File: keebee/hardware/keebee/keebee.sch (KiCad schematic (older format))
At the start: 2 parts

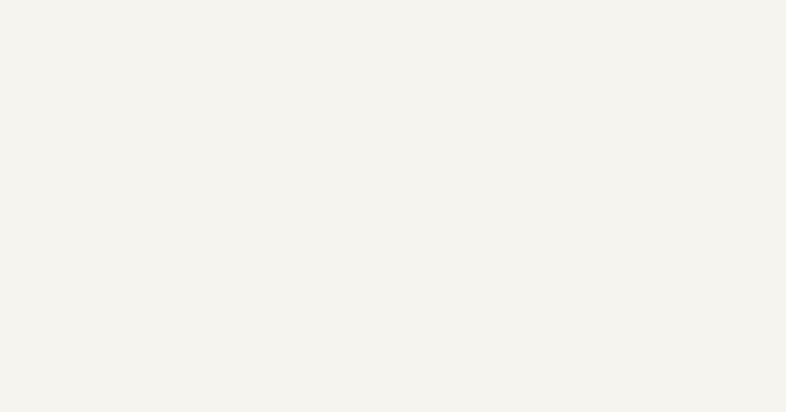
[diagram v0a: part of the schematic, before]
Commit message: Add in keebee power schematic
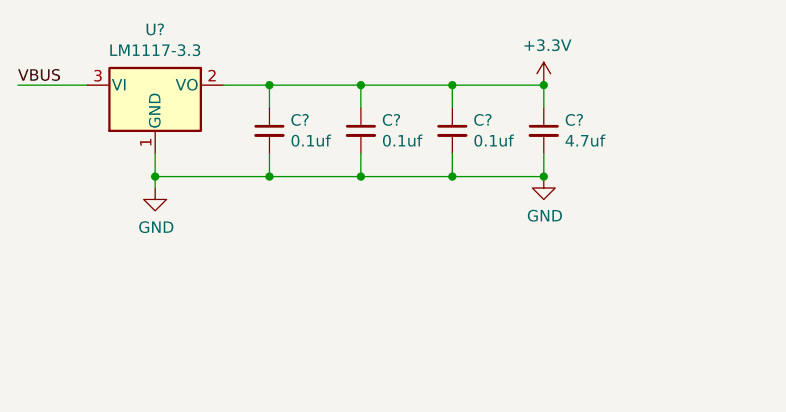
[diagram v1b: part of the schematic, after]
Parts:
- added C? (x3): 0.1uf, symbol Device:C_Small
- added C?: 4.7uf, symbol Device:C_Small
- added U?: LM1117-3.3, symbol Regulator_Linear:LM1117-3.3
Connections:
- net +3V3: now also C?.1, C?.1, C?.1, C?.1, U?.2 (VO)
- net GND: now also C?.2, C?.2, C?.2, C?.2, U?.1 (GND)
- net VBUS: now also U?.3 (VI)
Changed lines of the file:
@@
 Text Label 4700 3500 0    50   ~ 0
 ROW0
+$Comp
+L Regulator_Linear:LM1117-3.3 U?
+U 1 1 5B310EFD
+P 2050 1150
+F 0 "U?" H 2050 1392 50  0000 C CNN
+F 1 "LM1117-3.3" H 2050 1301 50  0000 C CNN
+F 2 "" H 2050 1150 50  0001 C CNN
+F 3 "http://www.ti.com/lit/ds/symlink/lm1117.pdf" H 2050 1150 50  0001 C CNN
+	1    2050 1150
+	1    0    0    -1
+$EndComp
+Wire Wire Line
+	1750 1150 1450 1150
+Text Label 1450 1150 0    50   ~ 0
+VBUS
+$Comp
+L power:+3.3V #PWR?
+U 1 1 5B312C80
+P 3750 1150
+F 0 "#PWR?" H 3750 1000 50  0001 C CNN
+F 1 "+3.3V" H 3765 1323 50  0000 C CNN
+F 2 "" H 3750 1150 50  0001 C CNN
+F 3 "" H 3750 1150 50  0001 C CNN
+	1    3750 1150
+	1    0    0    -1
+$EndComp
+Wire Wire Line
+	2050 1450 2050 1550
+$Comp
+L power:GND #PWR?
+U 1 1 5B313FEA
+P 2050 1600
+F 0 "#PWR?" H 2050 1350 50  0001 C CNN
+F 1 "GND" H 2055 1427 50  0000 C CNN
+F 2 "" H 2050 1600 50  0001 C CNN
+F 3 "" H 2050 1600 50  0001 C CNN
+	1    2050 1600
+	1    0    0    -1
+$EndComp
+Connection ~ 2050 1550
+Wire Wire Line
+	2050 1550 2050 1600
+$Comp
+L power:GND #PWR?
+U 1 1 5B31724A
+P 3750 1550
+F 0 "#PWR?" H 3750 1300 50  0001 C CNN
+F 1 "GND" H 3755 1377 50  0000 C CNN
+F 2 "" H 3750 1550 50  0001 C CNN
+F 3 "" H 3750 1550 50  0001 C CNN
+	1    3750 1550
+	1    0    0    -1
+$EndComp
+$Comp
+L Device:C_Small C?
+U 1 1 5B317DA6
+P 2550 1350
+F 0 "C?" H 2642 1396 50  0000 L CNN
+F 1 "0.1uf" H 2642 1305 50  0000 L CNN
+F 2 "" H 2550 1350 50  0001 C CNN
+F 3 "~" H 2550 1350 50  0001 C CNN
+	1    2550 1350
+	1    0    0    -1
+$EndComp
+$Comp
+L Device:C_Small C?
+U 1 1 5B317DF6
+P 2950 1350
+F 0 "C?" H 3042 1396 50  0000 L CNN
+F 1 "0.1uf" H 3042 1305 50  0000 L CNN
+F 2 "" H 2950 1350 50  0001 C CNN
+F 3 "~" H 2950 1350 50  0001 C CNN
+	1    2950 1350
+	1    0    0    -1
+$EndComp
+$Comp
+L Device:C_Small C?
+U 1 1 5B317E31
+P 3350 1350
+F 0 "C?" H 3442 1396 50  0000 L CNN
+F 1 "0.1uf" H 3442 1305 50  0000 L CNN
+F 2 "" H 3350 1350 50  0001 C CNN
+F 3 "~" H 3350 1350 50  0001 C CNN
+	1    3350 1350
+	1    0    0    -1
+$EndComp
+Wire Wire Line
+	2350 1150 2550 1150
+Wire Wire Line
+	2050 1550 2550 1550
+$Comp
+L Device:C_Small C?
+U 1 1 5B31D042
+P 3750 1350
+F 0 "C?" H 3842 1396 50  0000 L CNN
+F 1 "4.7uf" H 3842 1305 50  0000 L CNN
+F 2 "" H 3750 1350 50  0001 C CNN
+F 3 "~" H 3750 1350 50  0001 C CNN
+	1    3750 1350
+	1    0    0    -1
+$EndComp
+Wire Wire Line
+	3750 1150 3750 1250
+Connection ~ 3750 1150
+Wire Wire Line
+	3750 1450 3750 1550
+Connection ~ 3750 1550
+Wire Wire Line
+	3350 1250 3350 1150
+Connection ~ 3350 1150
+Wire Wire Line
+	3350 1150 3750 1150
+Wire Wire Line
+	3350 1450 3350 1550
+Connection ~ 3350 1550
+Wire Wire Line
+	3350 1550 3750 1550
+Wire Wire Line
+	2950 1250 2950 1150
+Connection ~ 2950 1150
+Wire Wire Line
+	2950 1150 3350 1150
+Wire Wire Line
+	2550 1250 2550 1150
+Connection ~ 2550 1150
+Wire Wire Line
+	2550 1150 2950 1150
+Wire Wire Line
+	2550 1450 2550 1550
+Connection ~ 2550 1550
+Wire Wire Line
+	2550 1550 2950 1550
+Wire Wire Line
+	2950 1450 2950 1550
+Connection ~ 2950 1550
+Wire Wire Line
+	2950 1550 3350 1550
 $EndSCHEMATC

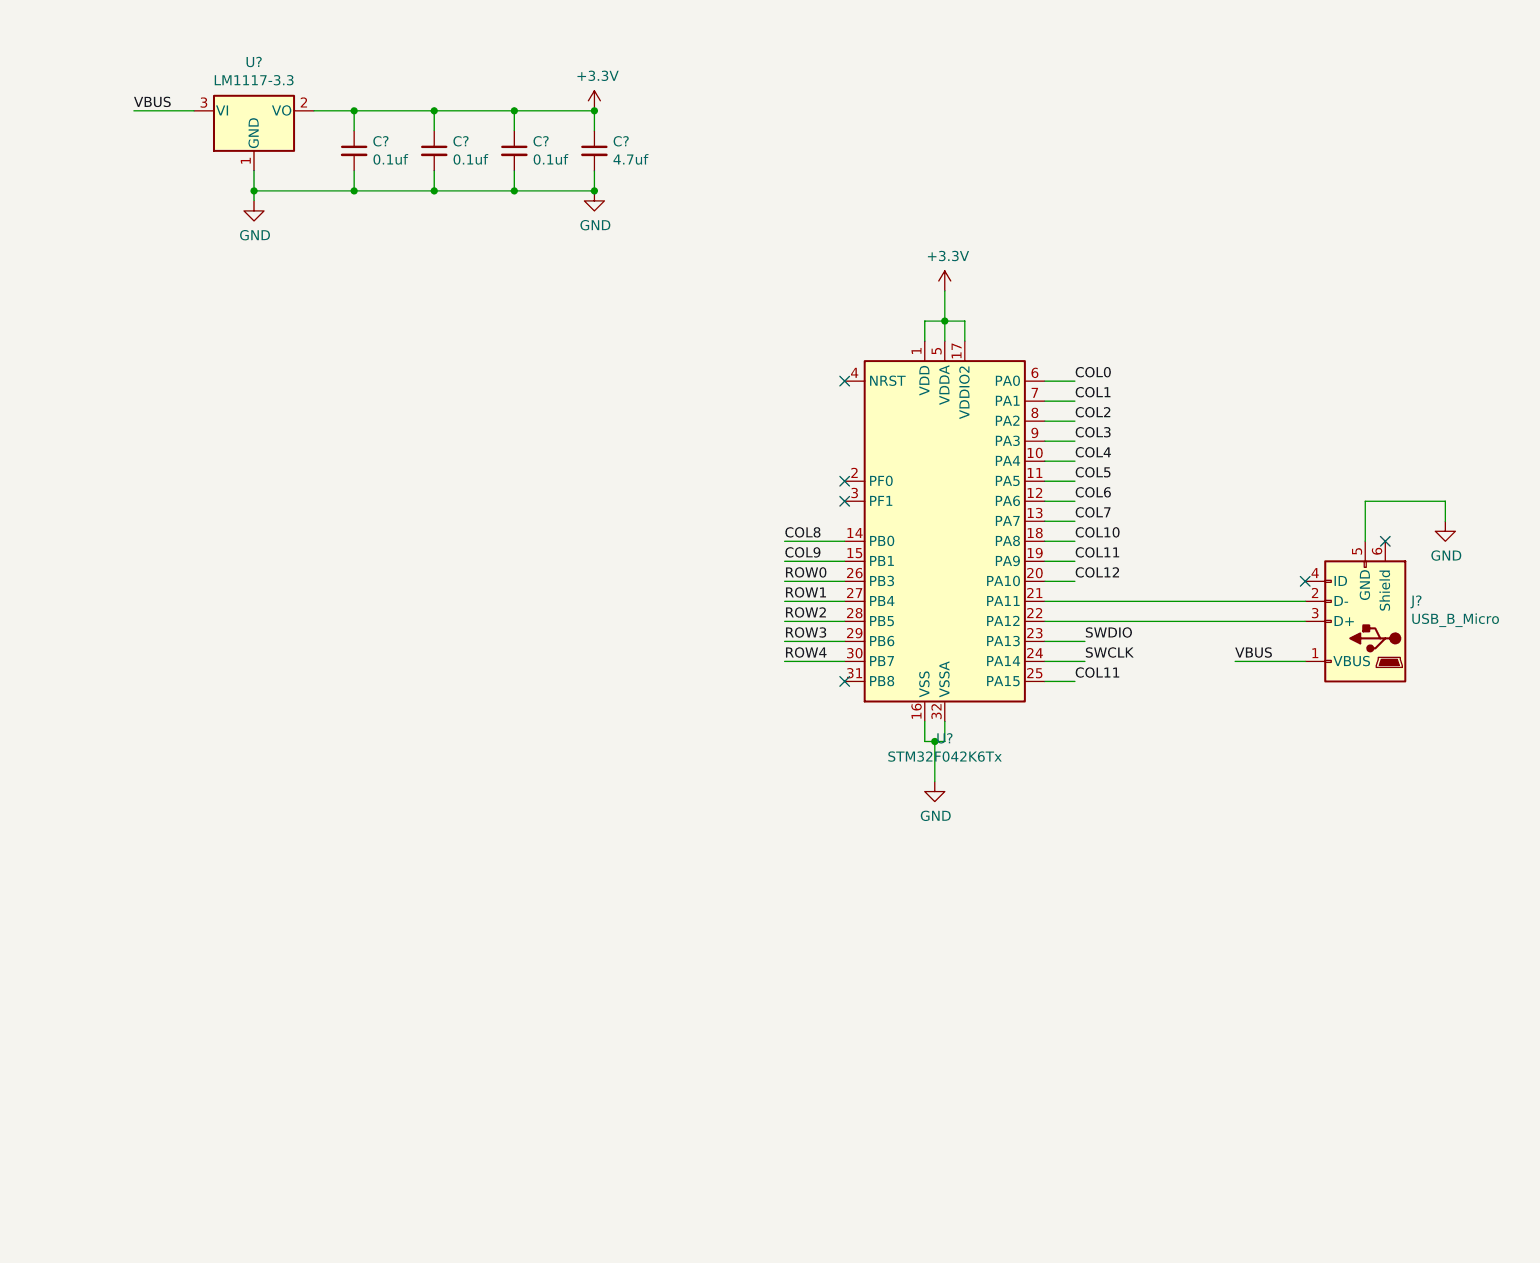
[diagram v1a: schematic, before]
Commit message: Add key matrix sub-sheet
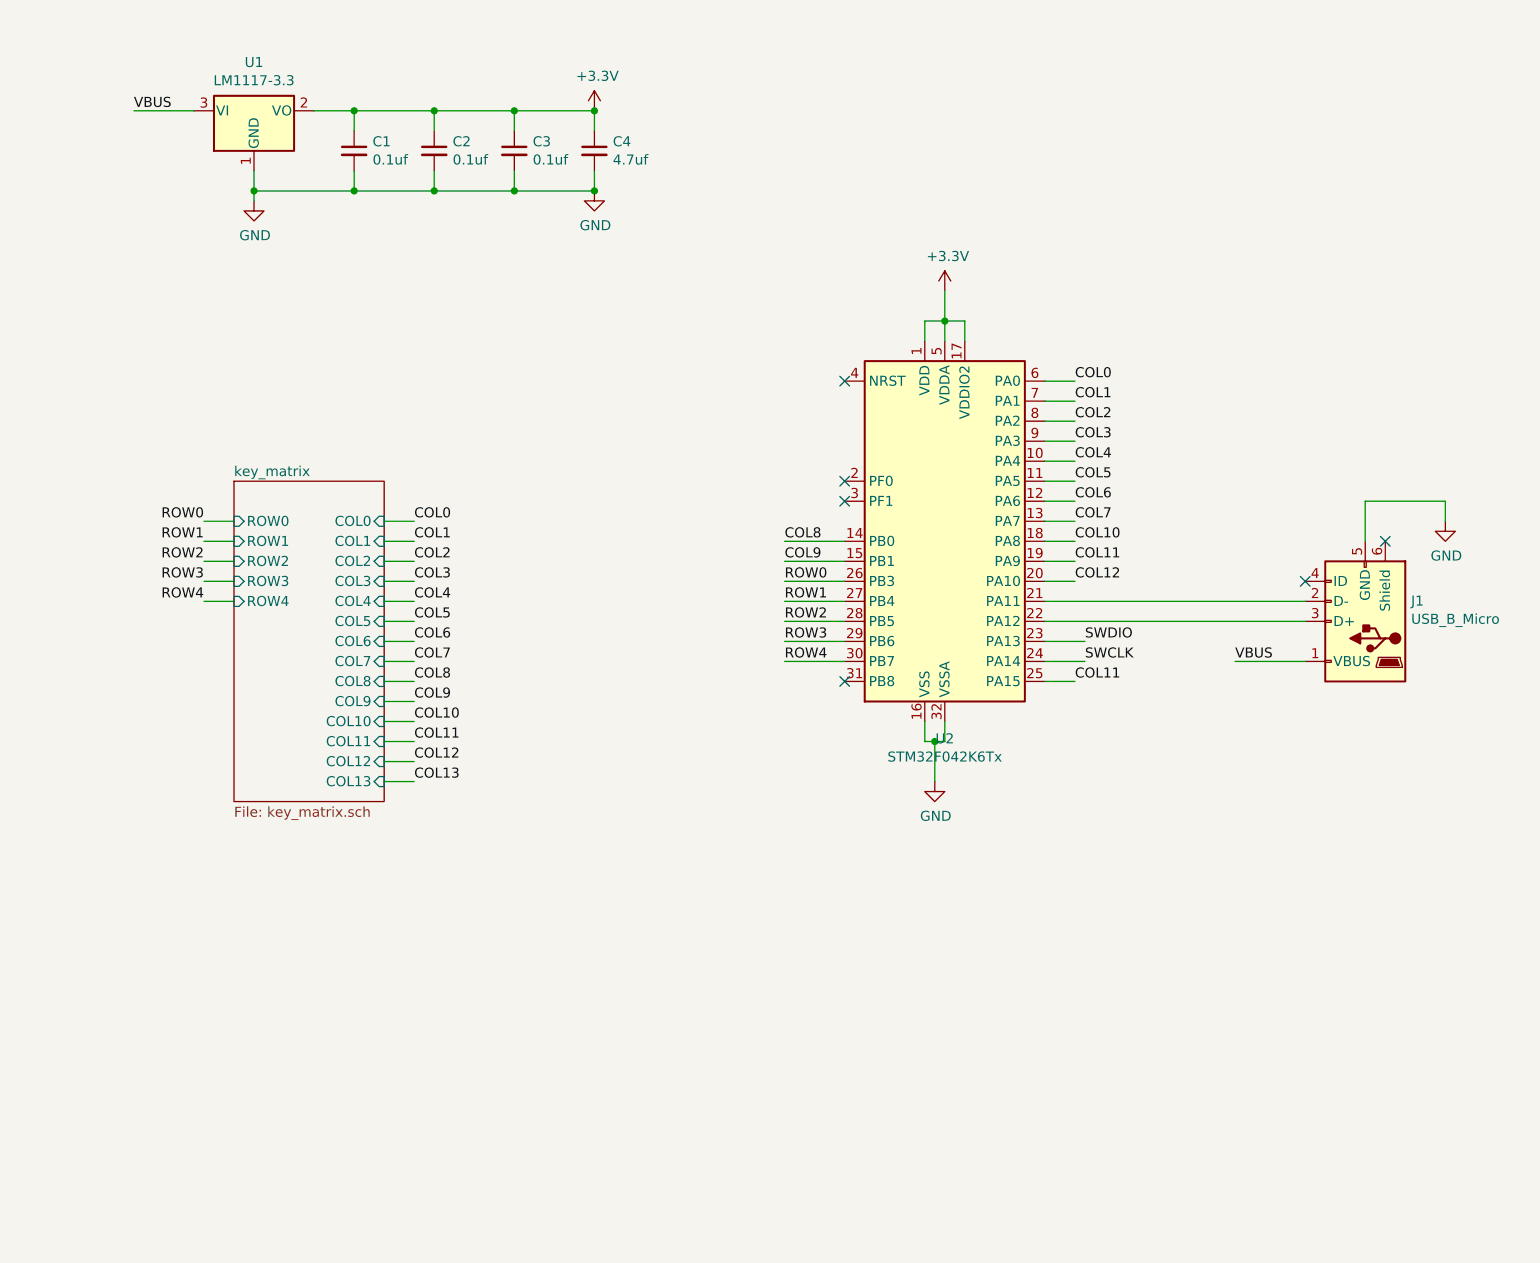
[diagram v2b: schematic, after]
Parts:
- gave numbers to parts that had none: 7
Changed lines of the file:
@@
 $Descr A4 11693 8268
 encoding utf-8
-Sheet 1 1
+Sheet 1 2
 Title ""
 Date ""
@@
 $EndDescr
 $Comp
-L MCU_ST_STM32F0:STM32F042K6Tx U?
+L MCU_ST_STM32F0:STM32F042K6Tx U2
 U 1 1 5B304C68
 P 5500 3200
-F 0 "U?" H 5500 2114 50  0000 C CNN
+F 0 "U2" H 5500 2114 50  0000 C CNN
 F 1 "STM32F042K6Tx" H 5500 2023 50  0000 C CNN
 F 2 "Package_QFP:LQFP-32_7x7mm_P0.8mm" H 5100 2300 50  0001 R CNN
@@
 	5450 4300 5500 4300
 $Comp
-L power:GND #PWR?
+L power:GND #PWR0101
 U 1 1 5B304DF2
 P 5450 4500
-F 0 "#PWR?" H 5450 4250 50  0001 C CNN
+F 0 "#PWR0101" H 5450 4250 50  0001 C CNN
 F 1 "GND" H 5455 4327 50  0000 C CNN
 F 2 "" H 5450 4500 50  0001 C CNN
@@
 	5500 2200 5500 2050
 $Comp
-L power:+3.3V #PWR?
+L power:+3.3V #PWR0102
 U 1 1 5B304F70
 P 5500 2050
-F 0 "#PWR?" H 5500 1900 50  0001 C CNN
+F 0 "#PWR0102" H 5500 1900 50  0001 C CNN
 F 1 "+3.3V" H 5515 2223 50  0000 C CNN
 F 2 "" H 5500 2050 50  0001 C CNN
@@
 SWCLK
 $Comp
-L Connector:USB_B_Micro J?
+L Connector:USB_B_Micro J1
 U 1 1 5B305155
 P 7600 3700
-F 0 "J?" H 7371 3598 50  0000 R CNN
+F 0 "J1" H 7371 3598 50  0000 R CNN
 F 1 "USB_B_Micro" H 7371 3689 50  0000 R CNN
 F 2 "" H 7750 3650 50  0001 C CNN
@@
 	8000 3100 8000 3200
 $Comp
-L power:GND #PWR?
+L power:GND #PWR0103
 U 1 1 5B3057C1
 P 8000 3200
-F 0 "#PWR?" H 8000 2950 50  0001 C CNN
+F 0 "#PWR0103" H 8000 2950 50  0001 C CNN
 F 1 "GND" H 8005 3027 50  0000 C CNN
 F 2 "" H 8000 3200 50  0001 C CNN
@@
 Wire Wire Line
 	4700 3400 5000 3400
-Wire Wire Line
-	4700 3500 5000 3500
-Wire Wire Line
-	4700 3600 5000 3600
-Wire Wire Line
-	4700 3700 5000 3700
-Wire Wire Line
-	4700 3800 5000 3800
-Wire Wire Line
-	4700 3900 5000 3900
 NoConn ~ 5000 2500
 NoConn ~ 5000 3000
@@
 ROW0
 $Comp
-L Regulator_Linear:LM1117-3.3 U?
+L Regulator_Linear:LM1117-3.3 U1
 U 1 1 5B310EFD
 P 2050 1150
-F 0 "U?" H 2050 1392 50  0000 C CNN
+F 0 "U1" H 2050 1392 50  0000 C CNN
 F 1 "LM1117-3.3" H 2050 1301 50  0000 C CNN
 F 2 "" H 2050 1150 50  0001 C CNN
@@
 VBUS
 $Comp
-L power:+3.3V #PWR?
+L power:+3.3V #PWR0104
 U 1 1 5B312C80
 P 3750 1150
-F 0 "#PWR?" H 3750 1000 50  0001 C CNN
+F 0 "#PWR0104" H 3750 1000 50  0001 C CNN
 F 1 "+3.3V" H 3765 1323 50  0000 C CNN
 F 2 "" H 3750 1150 50  0001 C CNN
@@
 	2050 1450 2050 1550
 $Comp
-L power:GND #PWR?
+L power:GND #PWR0105
 U 1 1 5B313FEA
 P 2050 1600
-F 0 "#PWR?" H 2050 1350 50  0001 C CNN
+F 0 "#PWR0105" H 2050 1350 50  0001 C CNN
 F 1 "GND" H 2055 1427 50  0000 C CNN
 F 2 "" H 2050 1600 50  0001 C CNN
@@
 	2050 1550 2050 1600
 $Comp
-L power:GND #PWR?
+L power:GND #PWR0106
 U 1 1 5B31724A
 P 3750 1550
-F 0 "#PWR?" H 3750 1300 50  0001 C CNN
+F 0 "#PWR0106" H 3750 1300 50  0001 C CNN
 F 1 "GND" H 3755 1377 50  0000 C CNN
 F 2 "" H 3750 1550 50  0001 C CNN
@@
 $EndComp
 $Comp
-L Device:C_Small C?
+L Device:C_Small C1
 U 1 1 5B317DA6
 P 2550 1350
-F 0 "C?" H 2642 1396 50  0000 L CNN
+F 0 "C1" H 2642 1396 50  0000 L CNN
 F 1 "0.1uf" H 2642 1305 50  0000 L CNN
 F 2 "" H 2550 1350 50  0001 C CNN
@@
 $EndComp
 $Comp
-L Device:C_Small C?
+L Device:C_Small C2
 U 1 1 5B317DF6
 P 2950 1350
-F 0 "C?" H 3042 1396 50  0000 L CNN
+F 0 "C2" H 3042 1396 50  0000 L CNN
 F 1 "0.1uf" H 3042 1305 50  0000 L CNN
 F 2 "" H 2950 1350 50  0001 C CNN
@@
 $EndComp
 $Comp
-L Device:C_Small C?
+L Device:C_Small C3
 U 1 1 5B317E31
 P 3350 1350
-F 0 "C?" H 3442 1396 50  0000 L CNN
+F 0 "C3" H 3442 1396 50  0000 L CNN
 F 1 "0.1uf" H 3442 1305 50  0000 L CNN
 F 2 "" H 3350 1350 50  0001 C CNN
@@
 	2050 1550 2550 1550
 $Comp
-L Device:C_Small C?
+L Device:C_Small C4
 U 1 1 5B31D042
 P 3750 1350
-F 0 "C?" H 3842 1396 50  0000 L CNN
+F 0 "C4" H 3842 1396 50  0000 L CNN
 F 1 "4.7uf" H 3842 1305 50  0000 L CNN
 F 2 "" H 3750 1350 50  0001 C CNN
@@
 Wire Wire Line
 	2950 1550 3350 1550
+$Sheet
+S 1950 3000 750  1600
+U 5B32407D
+F0 "key_matrix" 50
+F1 "key_matrix.sch" 50
+F2 "ROW0" I L 1950 3200 50
+F3 "ROW1" I L 1950 3300 50
+F4 "ROW2" I L 1950 3400 50
+F5 "ROW3" I L 1950 3500 50
+F6 "ROW4" I L 1950 3600 50
+F7 "COL0" I R 2700 3200 50
+F8 "COL1" I R 2700 3300 50
+F9 "COL2" I R 2700 3400 50
+F10 "COL3" I R 2700 3500 50
+F11 "COL4" I R 2700 3600 50
+F12 "COL5" I R 2700 3700 50
+F13 "COL6" I R 2700 3800 50
+F14 "COL7" I R 2700 3900 50
+F15 "COL8" I R 2700 4000 50
+F16 "COL9" I R 2700 4100 50
+F17 "COL10" I R 2700 4200 50
+F18 "COL11" I R 2700 4300 50
+F19 "COL12" I R 2700 4400 50
+F20 "COL13" I R 2700 4500 50
+$EndSheet
+Wire Wire Line
+	2850 3200 2700 3200
+Text Label 2850 3200 0    50   ~ 0
+COL0
+Wire Wire Line
+	2850 3300 2700 3300
+Text Label 2850 3300 0    50   ~ 0
+COL1
+Wire Wire Line
+	2850 3400 2700 3400
+Text Label 2850 3400 0    50   ~ 0
+COL2
+Wire Wire Line
+	2850 3500 2700 3500
+Text Label 2850 3500 0    50   ~ 0
+COL3
+Wire Wire Line
+	2850 3600 2700 3600
+Text Label 2850 3600 0    50   ~ 0
+COL4
+Wire Wire Line
+	2850 3700 2700 3700
+Text Label 2850 3700 0    50   ~ 0
+COL5
+Wire Wire Line
+	2850 3800 2700 3800
+Text Label 2850 3800 0    50   ~ 0
+COL6
+Wire Wire Line
+	2850 3900 2700 3900
+Text Label 2850 3900 0    50   ~ 0
+COL7
+Wire Wire Line
+	2850 4000 2700 4000
+Text Label 2850 4000 0    50   ~ 0
+COL8
+Wire Wire Line
+	2850 4100 2700 4100
+Text Label 2850 4100 0    50   ~ 0
+COL9
+Wire Wire Line
+	2850 4200 2700 4200
+Text Label 2850 4200 0    50   ~ 0
+COL10
+Wire Wire Line
+	2850 4300 2700 4300
+Text Label 2850 4300 0    50   ~ 0
+COL11
+Wire Wire Line
+	2850 4400 2700 4400
+Text Label 2850 4400 0    50   ~ 0
+COL12
+Wire Wire Line
+	2850 4500 2700 4500
+Text Label 2850 4500 0    50   ~ 0
+COL13
+Wire Wire Line
+	4700 3500 5000 3500
+Wire Wire Line
+	4700 3600 5000 3600
+Wire Wire Line
+	4700 3700 5000 3700
+Wire Wire Line
+	4700 3800 5000 3800
+Wire Wire Line
+	4700 3900 5000 3900
+Wire Wire Line
+	1950 3200 1800 3200
+Text Label 1800 3200 2    50   ~ 0
+ROW0
+Wire Wire Line
+	1950 3300 1800 3300
+Text Label 1800 3300 2    50   ~ 0
+ROW1
+Wire Wire Line
+	1950 3400 1800 3400
+Text Label 1800 3400 2    50   ~ 0
+ROW2
+Wire Wire Line
+	1950 3500 1800 3500
+Text Label 1800 3500 2    50   ~ 0
+ROW3
+Wire Wire Line
+	1950 3600 1800 3600
+Text Label 1800 3600 2    50   ~ 0
+ROW4
 $EndSCHEMATC
